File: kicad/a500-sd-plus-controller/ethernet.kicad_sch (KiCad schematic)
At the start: 24 parts, among them J5 RJ45, U10 ENC28J60x-SS, Y2 25.0MHz

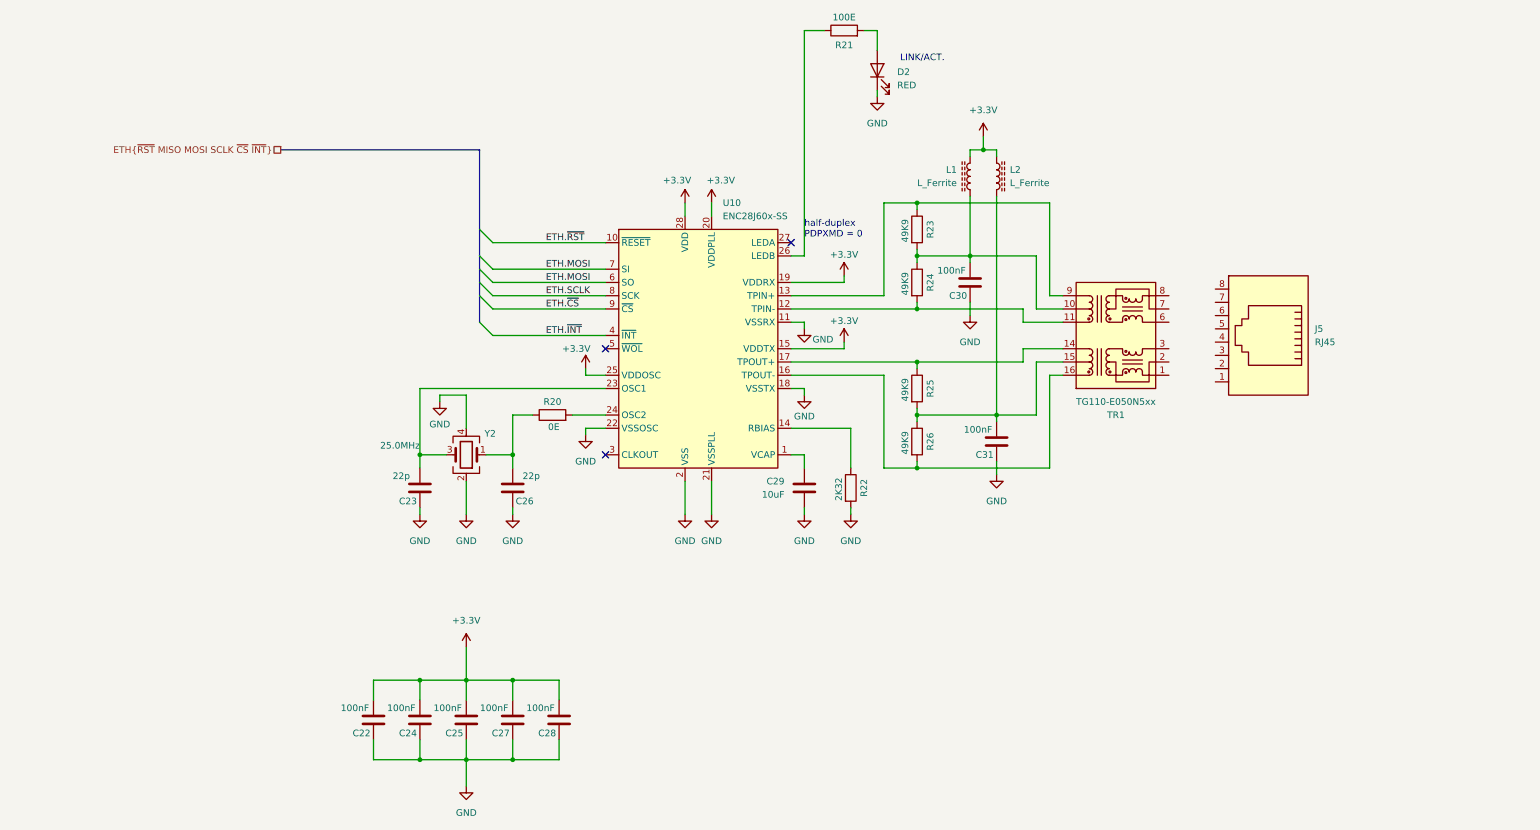
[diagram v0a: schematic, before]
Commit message: routing completely done
todo: review footprints and cleanup silkscreen
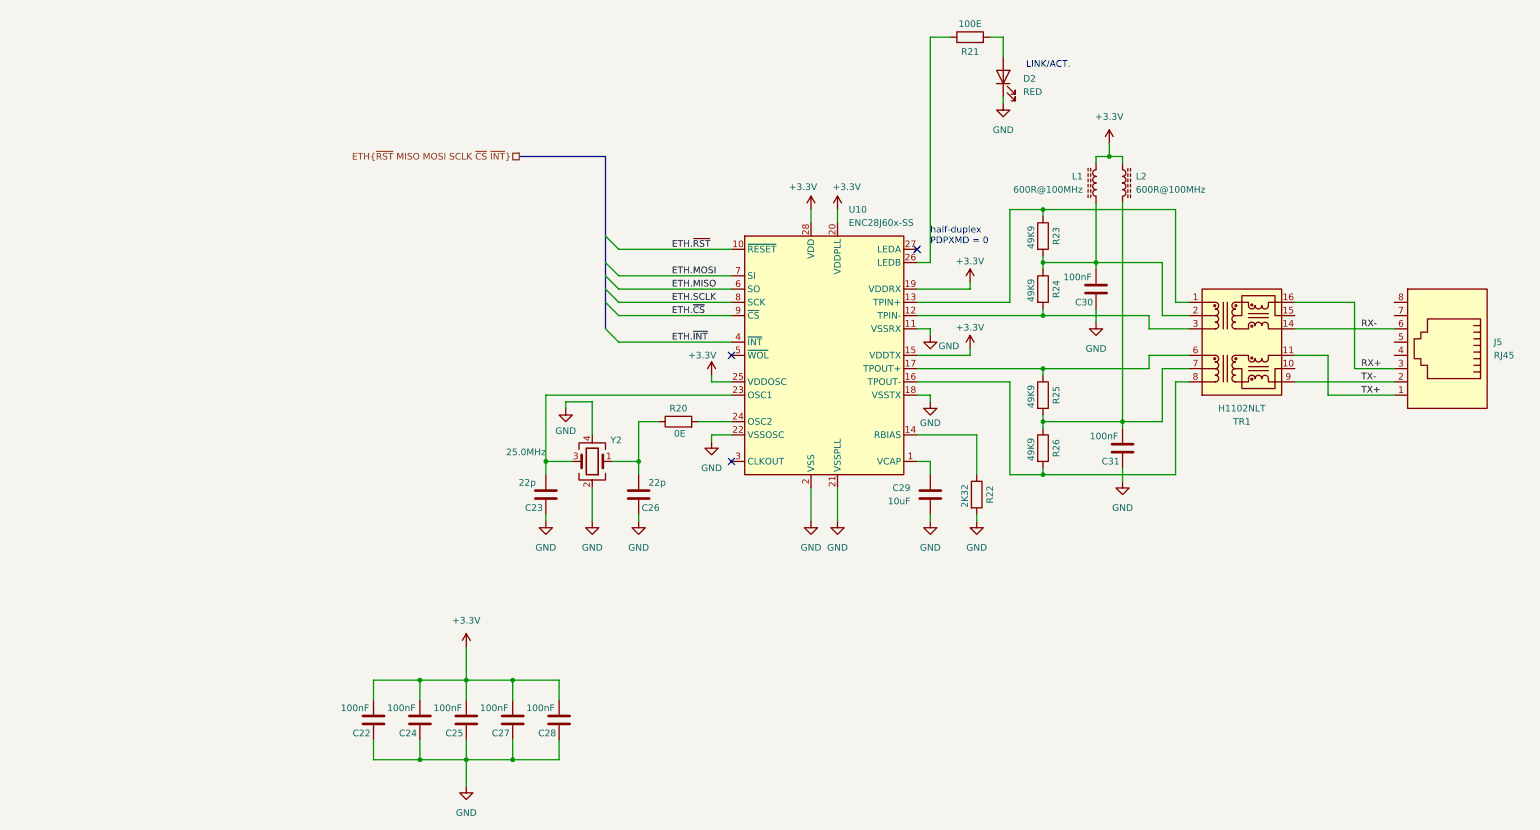
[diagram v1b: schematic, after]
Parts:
- removed TR1: TG110-E050N5xx, Transformer_SMD:Transformer_Ethernet_Halo_N5_SO-16_7.11x12.7mm, symbol Transformer:TG110-E050N5xx
- added TR1: H1102NLT, Transformer_SMD:Transformer_Ethernet_Bourns_PT61017PEL, symbol Transformer:PT61017PEL
- J5: footprint Connector_RJ:RJ45_Amphenol_54602-x08_Horizontal -> Library:R-RJ45R08P-A004; MPN (none) -> R-RJ45R08P-A004
- L1, L2: value L_Ferrite -> 600R@100MHz; MPN (none) -> GZ2012D601TF
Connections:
- net ETH.MOSI: no longer U10.6 (SO)
- net at R25.1, U10.17 (TPOUT+): now also TR1.6 (RD+)
- net at C31.1, L2.2, R25.2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: now also TR1.7 (C_RD)
- net at C30.1, L1.2, R23.2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: now also TR1.2 (C_TD)
- net TX+: now reaches J5.1
- net TX+: now also TR1.11 (RX+)
- net TX-: now reaches J5.2
- net TX-: now also TR1.9 (RX-)
- net RX+: now reaches J5.3
- net RX+: now also TR1.16 (TX+)
- net RX-: now reaches J5.6
- net RX-: now also TR1.14 (TX-)
- net at R24.2, U10.12 (TPIN-): now also TR1.3 (TD-)
- net at R26.2, U10.16 (TPOUT-): now also TR1.8 (RD-)
- net at R23.1, U10.13 (TPIN+): now also TR1.1 (TD+)
- new net ETH.MISO: U10.6 (SO)
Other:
- moved on the sheet: C23, C26, C29, C30, C31, D2, J5, L1, L2, R20, R21, R22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

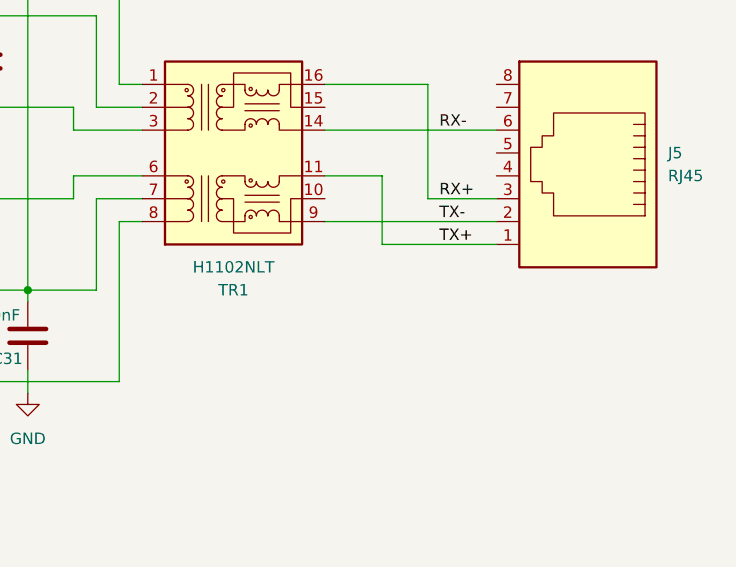
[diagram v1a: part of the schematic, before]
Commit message: cleaned up silkscreen and 3D models
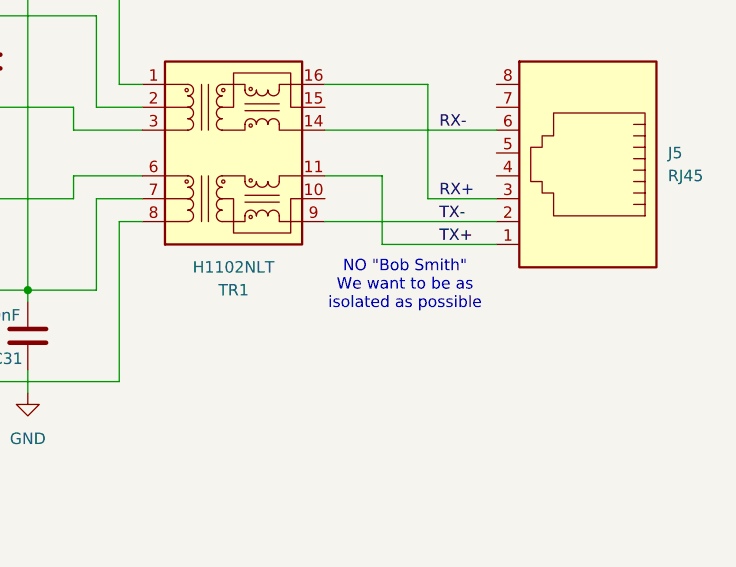
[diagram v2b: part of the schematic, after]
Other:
- note added: "NO "Bob Smith" We want to be as isolated as possible"
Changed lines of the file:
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@@
+		)
+	)
+	(text "NO \"Bob Smith\"\nWe want to be as \nisolated as possible"
+		(exclude_from_sim no)
+		(at 231.14 103.632 0)
+		(effects
+			(font
+				(size 1.27 1.27)
+			)
 		)
 	)

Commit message: PCB done, this version has been sent to fabrication
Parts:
- added R27: 68K, Resistor_SMD:R_0603_1608Metric, symbol Device:R
- C22, C24, C25, C27, C28, C30, C31: LCSC Part # (none) -> C14663; Quantity (none) -> ${QUANTITY}
- C23, C26: value 22p -> 22pF; LCSC Part # (none) -> C1653; Quantity (none) -> ${QUANTITY}
- C29: LCSC Part # (none) -> C15850; Quantity (none) -> ${QUANTITY}
- D2: LCSC Part # (none) -> C84256; Quantity (none) -> ${QUANTITY}
- J5: LCSC Part # (none) -> C385834; Quantity (none) -> ${QUANTITY}
- L1, L2: LCSC Part # (none) -> C1017; Quantity (none) -> ${QUANTITY}
- R20: value 0E -> 0R; LCSC Part # (none) -> C21189; Quantity (none) -> ${QUANTITY}
- R21: value 100E -> 470R; LCSC Part # (none) -> C23179; Quantity (none) -> ${QUANTITY}
- R22: value 2K32 -> 2K4; LCSC Part # (none) -> C22940; Quantity (none) -> ${QUANTITY}
- R23, R24, R25, R26: value 49K9 -> 49R9; LCSC Part # (none) -> C23185; Quantity (none) -> ${QUANTITY}
- TR1: LCSC Part # (none) -> C18584; MPN (none) -> H1102NLT; Quantity (none) -> ${QUANTITY}
- U10: value ENC28J60x-SS -> ENC28J60; LCSC Part # (none) -> C411626; MPN (none) -> ENC28J60-I/SS; Quantity (none) -> ${QUANTITY}
- Y2: LCSC Part # (none) -> C9006; Quantity (none) -> ${QUANTITY}
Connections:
- net GND: now also R27.2
- net at R22.1, U10.14 (RBIAS): now also R27.1
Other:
- note added: "2K32"
- moved on the sheet: C23, C26, C29, C30, C31, D2, J5, L1, L2, R20, R21, R22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
